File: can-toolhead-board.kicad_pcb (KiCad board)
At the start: 4 copper layers, 51 x 36.9 mm, 100 parts, among them J1 MF3-2x2P, J10 PH-2P, J11 PH-2P, J12 PH-2P, J13 PH-2P, J14 PH-2P, J15 PH-3P, J2 USB_C_Receptacle_USB2.0, J3 SH-6P, J4 PH-2P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

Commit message: Lots of little tweaks and simplifications
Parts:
- D4: moved to F.Cu
- JP1: value Jumper_2_Open -> SolderJumper_2_Bridged
- JP3, JP4: value Jumper_3_Open -> SolderJumper_3_Open
- R10, R9: value 22K -> 100K
- R14: value 22K -> 100K; moved to B.Cu
- R4: value 1M -> 100K
- moved D4 23.1 mm to (90.1, 100.8)
- moved R14 11.0 mm to (107.8, 100.6), turned to 0 degrees
- moved R7 10.5 mm to (86.1, 104.5), turned to -90 degrees
- moved C11 10.3 mm to (95.7, 87.1)
- moved R30 7.36 mm to (80.8, 110.4), turned to 90 degrees
- moved R22 5.95 mm to (116.8, 108.1), turned to -90 degrees
- moved C23 5.25 mm to (118.8, 108.1)
- moved R23 4.66 mm to (117.8, 108.1), turned to 90 degrees
- moved C9 2.69 mm to (107.3, 91.5)
- moved JP1 2.62 mm to (120.3, 104.1)
- moved D1 2.15 mm to (106.0, 88.9)
- moved R1 2.06 mm to (118.6, 106.5)
- moved JP2 1.93 mm to (109.2, 88.8), turned to 135 degrees
- moved R17 1.80 mm to (88.4, 102.0), turned to 90 degrees
- moved U7 1.51 mm to (111.1, 98.6), turned to 135 degrees
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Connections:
- JP1 pad 1: CANL -> CANH
- R1 pad 1: CANH -> CANL
- U4 pad 20: PROBE -> unconnected-(U4-PC6-Pad20)
- U4 pad 21: unconnected-(U4-PA10/UCPD1_DBCC2-Pad21) -> PROBE
- U6 pad 25: GND -> unconnected-(U6-NC-Pad25)
- U7 pad 4: USB_D- -> USB_D+
- U7 pad 6: USB_D+ -> USB_D-
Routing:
- net HEFAN_SENSE: track 30.5 -> 3.87 mm, vias 2 -> 1
- net Net-(D4-K): track 26.0 -> 12.7 mm, vias 0 -> 2
- net /~{RST}: track 33.7 -> 23.8 mm
- net Net-(J2-SHIELD): track 22.0 -> 30.4 mm
- net +24V: track 33.9 -> 41.7 mm
- net /D-: track 15.2 -> 22.0 mm
- net GND: track 70.5 -> 77.2 mm
- net +3V3: track 33.9 -> 27.6 mm
- net CANL: track 10.2 -> 16.4 mm, vias 0 -> 2
- net USB_D-: track 48.4 -> 42.4 mm
- net USB_D+: track 49.0 -> 43.7 mm
- net /BOOT0: track 23.1 -> 17.8 mm, vias 0 -> 2
- net Net-(J4-Pin_2): track 13.4 -> 9.42 mm, vias 0 -> 1
- net PROBE: track 22.2 -> 18.3 mm, vias 2 -> 0
- net +5V: track 72.0 -> 75.7 mm, vias 3 -> 4
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- added copper zone on B.Cu, net GND
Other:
- board text added: "5V"
- board text added: "UTB36 ${PCB_VERSION}"
- board text removed: "5"
- board text removed: "CTB ${PCB_VERSION}"

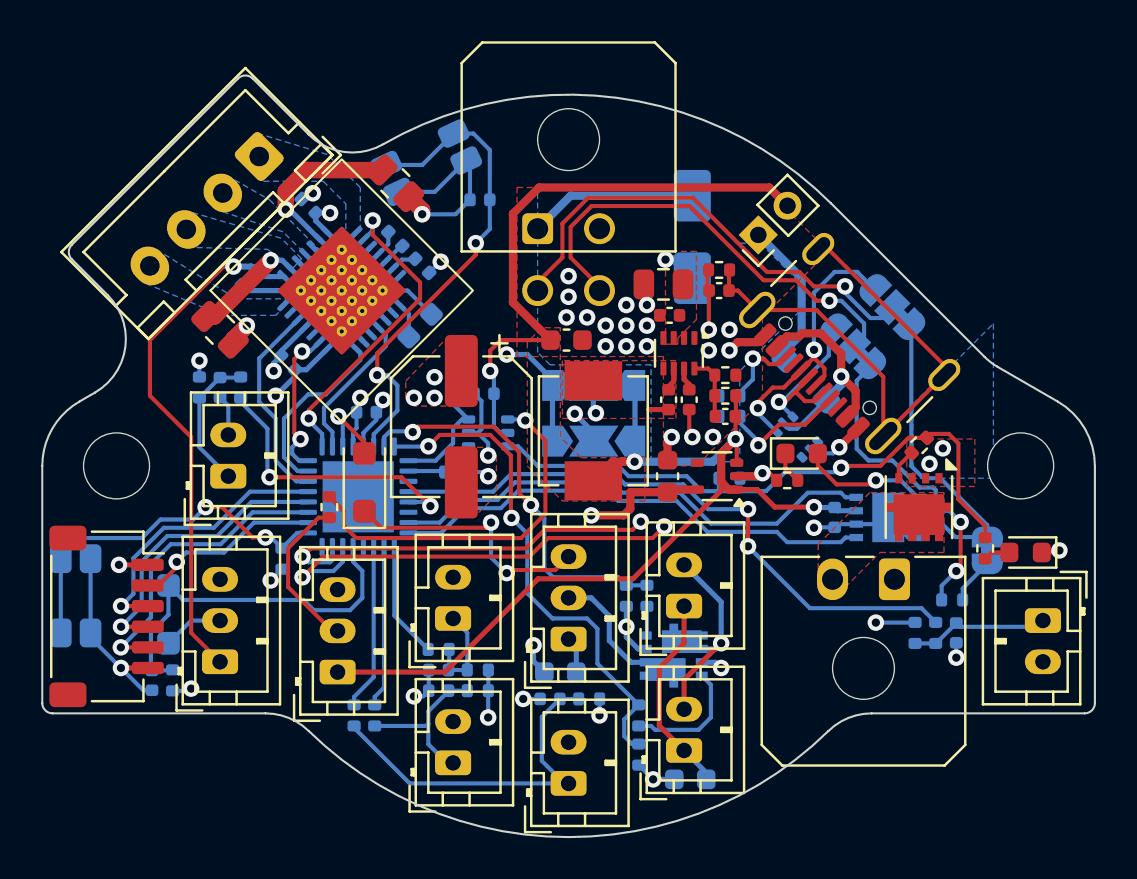
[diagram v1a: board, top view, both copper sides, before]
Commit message: Modify SPI connector pinout
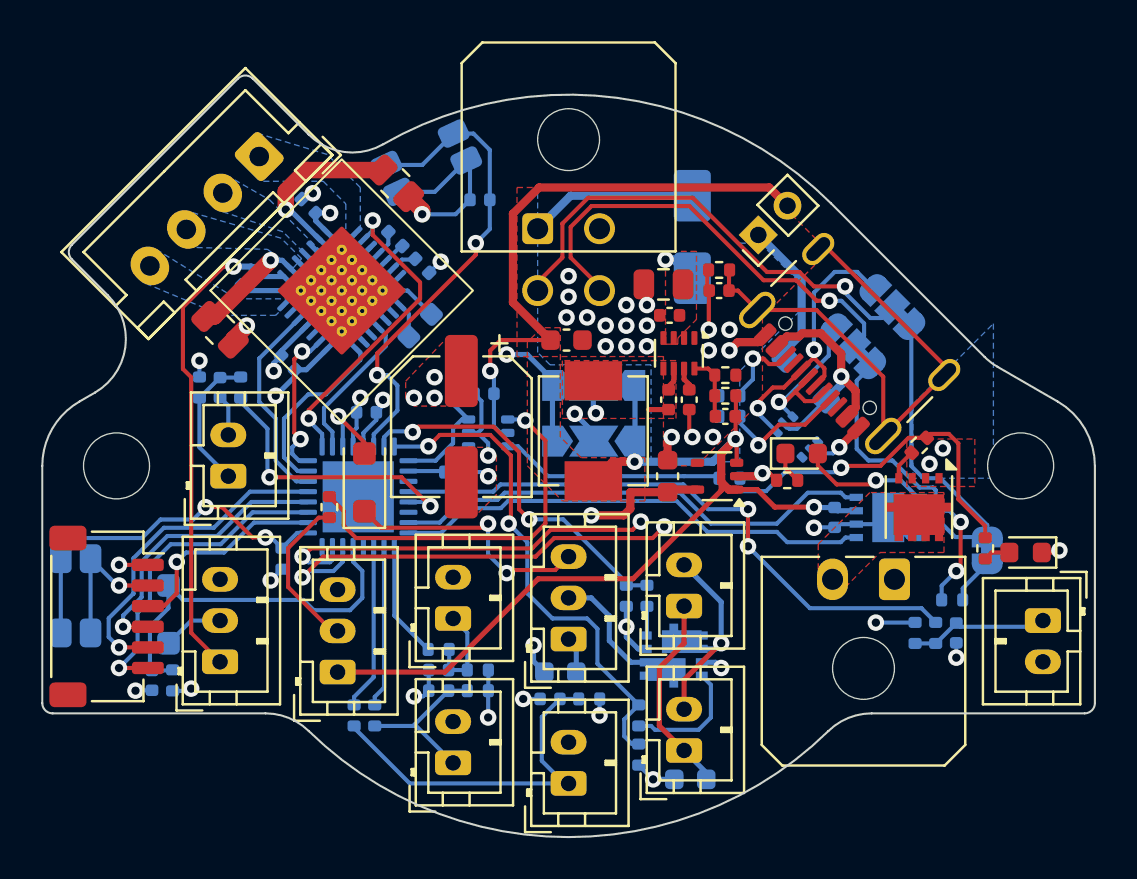
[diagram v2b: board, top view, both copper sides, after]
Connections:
- J3 pad 2: /~{SS} -> GND
- J3 pad 3: /MOSI -> /~{SS}
- J3 pad 5: /SCK -> /MOSI
- J3 pad 6: GND -> /SCK
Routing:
- net /MOSI: track 13.7 -> 16.2 mm
- net GND: track 77.2 -> 75.8 mm, vias 40 -> 41
- net +24V: track 41.7 -> 40.4 mm
- net /~{SS}: track 9.17 -> 10.3 mm
- net /SCK: track 14.6 -> 15.7 mm
- net PCFAN: track 19.2 -> 18.3 mm
- net Net-(R13-Pad1): track 29.8 -> 29.2 mm
